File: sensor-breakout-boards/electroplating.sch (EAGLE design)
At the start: 4 parts, among them X1 Type-A Receptacle, X2 Micro Type-B Receptacle

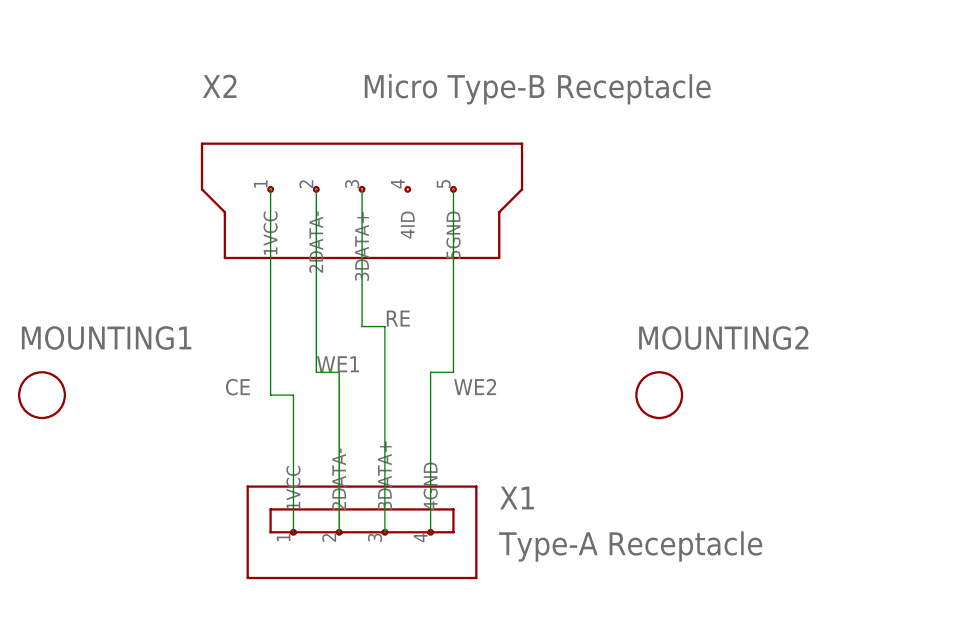
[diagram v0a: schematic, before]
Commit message: three breakout boards complete
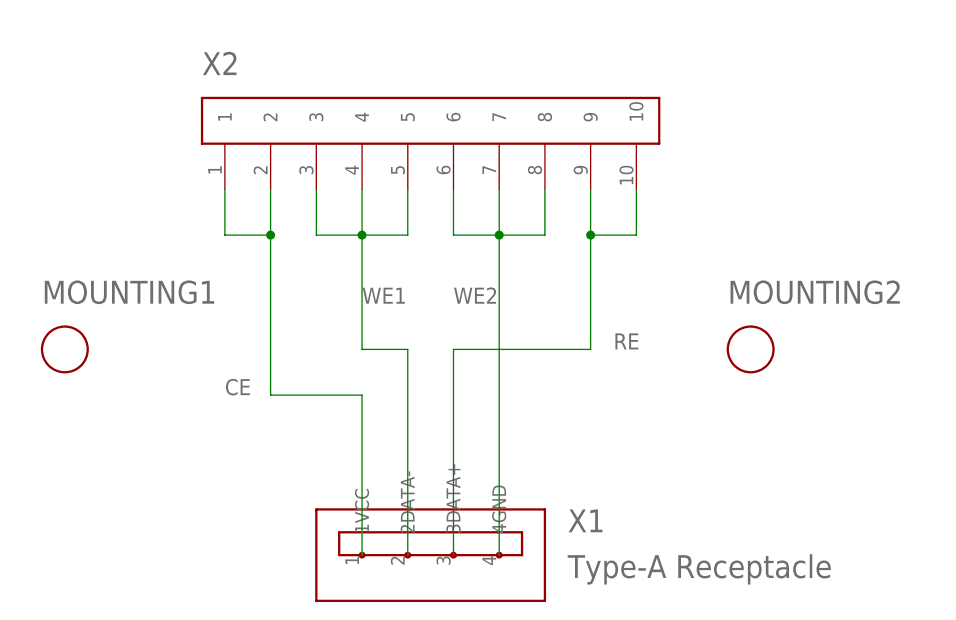
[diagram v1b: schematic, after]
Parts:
- X2: value Micro Type-B Receptacle -> 10-PIN-CONNECTOR; device sensor-breakout-boards:USB-MICRO-TYPE-B-RECEPTACLE -> sensor-breakout-boards:10-PIN-CONNECTOR
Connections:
- net CE: now also X2.1, X2.2; no longer X2.1VCC
- net RE: now also X2.10, X2.9; no longer X2.3DATA+
- net WE1: now also X2.3, X2.4, X2.5; no longer X2.2DATA-
- net WE2: now also X2.6, X2.7, X2.8; no longer X2.5GND
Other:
- moved on the sheet: MOUNTING1, MOUNTING2, X1
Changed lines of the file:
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@@
 <parts>
 <part name="X1" library="sensor-breakout-boards" deviceset="USB-TYPE-A-RECEPTACLE" device="" value="Type-A Receptacle"/>
-<part name="X2" library="sensor-breakout-boards" deviceset="USB-MICRO-TYPE-B-RECEPTACLE" device="" value="Micro Type-B Receptacle"/>
+<part name="X2" library="sensor-breakout-boards" deviceset="10-PIN-CONNECTOR" device=""/>
 <part name="MOUNTING1" library="sensor-breakout-boards" deviceset="M2-MOUNTING-HOLE" device=""/>
 <part name="MOUNTING2" library="sensor-breakout-boards" deviceset="M2-MOUNTING-HOLE" device=""/>
@@
 </plain>
 <instances>
-<instance part="X1" gate="G$1" x="43.18" y="17.78"/>
-<instance part="X2" gate="G$1" x="43.18" y="55.88"/>
-<instance part="MOUNTING1" gate="G$1" x="7.62" y="33.02"/>
-<instance part="MOUNTING2" gate="G$1" x="76.2" y="33.02"/>
+<instance part="X1" gate="G$1" x="50.8" y="15.24"/>
+<instance part="X2" gate="G$1" x="50.8" y="63.5"/>
+<instance part="MOUNTING1" gate="G$1" x="10.16" y="38.1"/>
+<instance part="MOUNTING2" gate="G$1" x="86.36" y="38.1"/>
 </instances>
 <busses>
@@
 <net name="CE" class="0">
 <segment>
+<pinref part="X2" gate="G$1" pin="1"/>
+<wire x1="27.94" y1="55.88" x2="27.94" y2="50.8" width="0.1524" layer="91"/>
+<wire x1="27.94" y1="50.8" x2="33.02" y2="50.8" width="0.1524" layer="91"/>
+<pinref part="X2" gate="G$1" pin="2"/>
+<wire x1="33.02" y1="50.8" x2="33.02" y2="55.88" width="0.1524" layer="91"/>
+<wire x1="33.02" y1="50.8" x2="33.02" y2="33.02" width="0.1524" layer="91"/>
+<junction x="33.02" y="50.8"/>
 <pinref part="X1" gate="G$1" pin="1VCC"/>
-<wire x1="35.56" y1="17.78" x2="35.56" y2="33.02" width="0.1524" layer="91"/>
-<wire x1="35.56" y1="33.02" x2="33.02" y2="33.02" width="0.1524" layer="91"/>
-<pinref part="X2" gate="G$1" pin="1VCC"/>
-<wire x1="33.02" y1="33.02" x2="33.02" y2="55.88" width="0.1524" layer="91"/>
+<wire x1="33.02" y1="33.02" x2="43.18" y2="33.02" width="0.1524" layer="91"/>
+<wire x1="43.18" y1="33.02" x2="43.18" y2="15.24" width="0.1524" layer="91"/>
 <label x="27.94" y="33.02" size="1.778" layer="95"/>
 </segment>
@@
 <net name="WE1" class="0">
 <segment>
-<pinref part="X2" gate="G$1" pin="2DATA-"/>
-<wire x1="38.1" y1="55.88" x2="38.1" y2="35.56" width="0.1524" layer="91"/>
+<pinref part="X2" gate="G$1" pin="3"/>
+<wire x1="38.1" y1="55.88" x2="38.1" y2="50.8" width="0.1524" layer="91"/>
+<wire x1="38.1" y1="50.8" x2="43.18" y2="50.8" width="0.1524" layer="91"/>
+<pinref part="X2" gate="G$1" pin="4"/>
+<wire x1="43.18" y1="50.8" x2="43.18" y2="55.88" width="0.1524" layer="91"/>
+<pinref part="X2" gate="G$1" pin="5"/>
+<wire x1="43.18" y1="50.8" x2="48.26" y2="50.8" width="0.1524" layer="91"/>
+<wire x1="48.26" y1="50.8" x2="48.26" y2="55.88" width="0.1524" layer="91"/>
+<junction x="43.18" y="50.8"/>
+<wire x1="43.18" y1="50.8" x2="43.18" y2="38.1" width="0.1524" layer="91"/>
 <pinref part="X1" gate="G$1" pin="2DATA-"/>
-<wire x1="38.1" y1="35.56" x2="40.64" y2="35.56" width="0.1524" layer="91"/>
-<wire x1="40.64" y1="35.56" x2="40.64" y2="17.78" width="0.1524" layer="91"/>
-<label x="38.1" y="35.56" size="1.778" layer="95"/>
+<wire x1="43.18" y1="38.1" x2="48.26" y2="38.1" width="0.1524" layer="91"/>
+<wire x1="48.26" y1="38.1" x2="48.26" y2="15.24" width="0.1524" layer="91"/>
+<label x="43.18" y="43.18" size="1.778" layer="95"/>
+</segment>
+</net>
+<net name="WE2" class="0">
+<segment>
+<pinref part="X2" gate="G$1" pin="6"/>
+<wire x1="53.34" y1="55.88" x2="53.34" y2="50.8" width="0.1524" layer="91"/>
+<wire x1="53.34" y1="50.8" x2="58.42" y2="50.8" width="0.1524" layer="91"/>
+<pinref part="X2" gate="G$1" pin="7"/>
+<wire x1="58.42" y1="50.8" x2="58.42" y2="55.88" width="0.1524" layer="91"/>
+<wire x1="58.42" y1="50.8" x2="63.5" y2="50.8" width="0.1524" layer="91"/>
+<junction x="58.42" y="50.8"/>
+<pinref part="X2" gate="G$1" pin="8"/>
+<wire x1="63.5" y1="50.8" x2="63.5" y2="55.88" width="0.1524" layer="91"/>
+<pinref part="X1" gate="G$1" pin="4GND"/>
+<wire x1="58.42" y1="50.8" x2="58.42" y2="15.24" width="0.1524" layer="91"/>
+<label x="53.34" y="43.18" size="1.778" layer="95"/>
 </segment>
 </net>
 <net name="RE" class="0">
 <segment>
-<pinref part="X2" gate="G$1" pin="3DATA+"/>
-<wire x1="43.18" y1="55.88" x2="43.18" y2="40.64" width="0.1524" layer="91"/>
+<pinref part="X2" gate="G$1" pin="9"/>
+<wire x1="68.58" y1="55.88" x2="68.58" y2="50.8" width="0.1524" layer="91"/>
+<wire x1="68.58" y1="50.8" x2="73.66" y2="50.8" width="0.1524" layer="91"/>
+<pinref part="X2" gate="G$1" pin="10"/>
+<wire x1="73.66" y1="50.8" x2="73.66" y2="55.88" width="0.1524" layer="91"/>
+<wire x1="68.58" y1="50.8" x2="68.58" y2="38.1" width="0.1524" layer="91"/>
+<junction x="68.58" y="50.8"/>
 <pinref part="X1" gate="G$1" pin="3DATA+"/>
-<wire x1="43.18" y1="40.64" x2="45.72" y2="40.64" width="0.1524" layer="91"/>
-<wire x1="45.72" y1="40.64" x2="45.72" y2="17.78" width="0.1524" layer="91"/>
-<label x="45.72" y="40.64" size="1.778" layer="95"/>
+<wire x1="68.58" y1="38.1" x2="53.34" y2="38.1" width="0.1524" layer="91"/>
+<wire x1="53.34" y1="38.1" x2="53.34" y2="15.24" width="0.1524" layer="91"/>
+<label x="71.12" y="38.1" size="1.778" layer="95"/>
 </segment>
 </net>
-<net name="WE2" class="0">
-<segment>
-<pinref part="X2" gate="G$1" pin="5GND"/>
-<wire x1="53.34" y1="55.88" x2="53.34" y2="35.56" width="0.1524" layer="91"/>
-<pinref part="X1" gate="G$1" pin="4GND"/>
-<wire x1="53.34" y1="35.56" x2="50.8" y2="35.56" width="0.1524" layer="91"/>
-<wire x1="50.8" y1="35.56" x2="50.8" y2="17.78" width="0.1524" layer="91"/>
-<label x="53.34" y="33.02" size="1.778" layer="95"/>
-</segment>
-</net>

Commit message: made changes discussed at meeting
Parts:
- added X3, X4, X5: 2-PIN-CONNECTOR, sensor-breakout-boards:2-PIN-CONNECTOR
- X2: value 10-PIN-CONNECTOR -> 2-PIN-CONNECTOR; device sensor-breakout-boards:10-PIN-CONNECTOR -> sensor-breakout-boards:2-PIN-CONNECTOR
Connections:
- net RE: now also X4.1, X4.2; no longer X2.10, X2.9
- net WE1: now also X1.4GND, X5.1, X5.2; no longer X1.2DATA-, X2.3, X2.4, X2.5
- net WE2: now also X1.2DATA-, X3.1, X3.2; no longer X1.4GND, X2.6, X2.7, X2.8
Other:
- moved on the sheet: MOUNTING1, MOUNTING2
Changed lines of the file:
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@@
 <parts>
 <part name="X1" library="sensor-breakout-boards" deviceset="USB-TYPE-A-RECEPTACLE" device="" value="Type-A Receptacle"/>
-<part name="X2" library="sensor-breakout-boards" deviceset="10-PIN-CONNECTOR" device=""/>
 <part name="MOUNTING1" library="sensor-breakout-boards" deviceset="M2-MOUNTING-HOLE" device=""/>
 <part name="MOUNTING2" library="sensor-breakout-boards" deviceset="M2-MOUNTING-HOLE" device=""/>
+<part name="X2" library="sensor-breakout-boards" deviceset="2-PIN-CONNECTOR" device=""/>
+<part name="X3" library="sensor-breakout-boards" deviceset="2-PIN-CONNECTOR" device=""/>
+<part name="X4" library="sensor-breakout-boards" deviceset="2-PIN-CONNECTOR" device=""/>
+<part name="X5" library="sensor-breakout-boards" deviceset="2-PIN-CONNECTOR" device=""/>
 </parts>
 <sheets>
@@
 <instances>
 <instance part="X1" gate="G$1" x="50.8" y="15.24"/>
-<instance part="X2" gate="G$1" x="50.8" y="63.5"/>
-<instance part="MOUNTING1" gate="G$1" x="10.16" y="38.1"/>
-<instance part="MOUNTING2" gate="G$1" x="86.36" y="38.1"/>
+<instance part="MOUNTING1" gate="G$1" x="10.16" y="20.32"/>
+<instance part="MOUNTING2" gate="G$1" x="83.82" y="30.48"/>
+<instance part="X2" gate="G$1" x="25.4" y="63.5"/>
+<instance part="X3" gate="G$1" x="40.64" y="63.5"/>
+<instance part="X4" gate="G$1" x="55.88" y="63.5"/>
+<instance part="X5" gate="G$1" x="71.12" y="63.5"/>
 </instances>
 <busses>
@@
 <net name="CE" class="0">
 <segment>
+<wire x1="27.94" y1="58.42" x2="27.94" y2="53.34" width="0.1524" layer="91"/>
+<pinref part="X1" gate="G$1" pin="1VCC"/>
+<wire x1="27.94" y1="53.34" x2="27.94" y2="33.02" width="0.1524" layer="91"/>
+<wire x1="27.94" y1="33.02" x2="43.18" y2="33.02" width="0.1524" layer="91"/>
+<wire x1="43.18" y1="33.02" x2="43.18" y2="15.24" width="0.1524" layer="91"/>
+<label x="22.86" y="48.26" size="1.778" layer="95"/>
+<pinref part="X2" gate="G$1" pin="2"/>
 <pinref part="X2" gate="G$1" pin="1"/>
-<wire x1="27.94" y1="55.88" x2="27.94" y2="50.8" width="0.1524" layer="91"/>
-<wire x1="27.94" y1="50.8" x2="33.02" y2="50.8" width="0.1524" layer="91"/>
-<pinref part="X2" gate="G$1" pin="2"/>
-<wire x1="33.02" y1="50.8" x2="33.02" y2="55.88" width="0.1524" layer="91"/>
-<wire x1="33.02" y1="50.8" x2="33.02" y2="33.02" width="0.1524" layer="91"/>
-<junction x="33.02" y="50.8"/>
-<pinref part="X1" gate="G$1" pin="1VCC"/>
-<wire x1="33.02" y1="33.02" x2="43.18" y2="33.02" width="0.1524" layer="91"/>
-<wire x1="43.18" y1="33.02" x2="43.18" y2="15.24" width="0.1524" layer="91"/>
-<label x="27.94" y="33.02" size="1.778" layer="95"/>
+<wire x1="22.86" y1="58.42" x2="22.86" y2="53.34" width="0.1524" layer="91"/>
+<wire x1="22.86" y1="53.34" x2="27.94" y2="53.34" width="0.1524" layer="91"/>
+<junction x="27.94" y="53.34"/>
+</segment>
+</net>
+<net name="WE2" class="0">
+<segment>
+<wire x1="43.18" y1="58.42" x2="43.18" y2="53.34" width="0.1524" layer="91"/>
+<pinref part="X1" gate="G$1" pin="2DATA-"/>
+<wire x1="43.18" y1="53.34" x2="43.18" y2="38.1" width="0.1524" layer="91"/>
+<wire x1="43.18" y1="38.1" x2="48.26" y2="38.1" width="0.1524" layer="91"/>
+<wire x1="48.26" y1="38.1" x2="48.26" y2="15.24" width="0.1524" layer="91"/>
+<label x="38.1" y="48.26" size="1.778" layer="95"/>
+<pinref part="X3" gate="G$1" pin="2"/>
+<pinref part="X3" gate="G$1" pin="1"/>
+<wire x1="38.1" y1="58.42" x2="38.1" y2="53.34" width="0.1524" layer="91"/>
+<wire x1="38.1" y1="53.34" x2="43.18" y2="53.34" width="0.1524" layer="91"/>
+<junction x="43.18" y="53.34"/>
 </segment>
 </net>
 <net name="WE1" class="0">
 <segment>
-<pinref part="X2" gate="G$1" pin="3"/>
-<wire x1="38.1" y1="55.88" x2="38.1" y2="50.8" width="0.1524" layer="91"/>
-<wire x1="38.1" y1="50.8" x2="43.18" y2="50.8" width="0.1524" layer="91"/>
-<pinref part="X2" gate="G$1" pin="4"/>
-<wire x1="43.18" y1="50.8" x2="43.18" y2="55.88" width="0.1524" layer="91"/>
-<pinref part="X2" gate="G$1" pin="5"/>
-<wire x1="43.18" y1="50.8" x2="48.26" y2="50.8" width="0.1524" layer="91"/>
-<wire x1="48.26" y1="50.8" x2="48.26" y2="55.88" width="0.1524" layer="91"/>
-<junction x="43.18" y="50.8"/>
-<wire x1="43.18" y1="50.8" x2="43.18" y2="38.1" width="0.1524" layer="91"/>
-<pinref part="X1" gate="G$1" pin="2DATA-"/>
-<wire x1="43.18" y1="38.1" x2="48.26" y2="38.1" width="0.1524" layer="91"/>
-<wire x1="48.26" y1="38.1" x2="48.26" y2="15.24" width="0.1524" layer="91"/>
-<label x="43.18" y="43.18" size="1.778" layer="95"/>
-</segment>
-</net>
-<net name="WE2" class="0">
-<segment>
-<pinref part="X2" gate="G$1" pin="6"/>
-<wire x1="53.34" y1="55.88" x2="53.34" y2="50.8" width="0.1524" layer="91"/>
-<wire x1="53.34" y1="50.8" x2="58.42" y2="50.8" width="0.1524" layer="91"/>
-<pinref part="X2" gate="G$1" pin="7"/>
-<wire x1="58.42" y1="50.8" x2="58.42" y2="55.88" width="0.1524" layer="91"/>
-<wire x1="58.42" y1="50.8" x2="63.5" y2="50.8" width="0.1524" layer="91"/>
-<junction x="58.42" y="50.8"/>
-<pinref part="X2" gate="G$1" pin="8"/>
-<wire x1="63.5" y1="50.8" x2="63.5" y2="55.88" width="0.1524" layer="91"/>
 <pinref part="X1" gate="G$1" pin="4GND"/>
-<wire x1="58.42" y1="50.8" x2="58.42" y2="15.24" width="0.1524" layer="91"/>
-<label x="53.34" y="43.18" size="1.778" layer="95"/>
+<wire x1="58.42" y1="38.1" x2="58.42" y2="15.24" width="0.1524" layer="91"/>
+<label x="68.58" y="48.26" size="1.778" layer="95"/>
+<pinref part="X5" gate="G$1" pin="1"/>
+<wire x1="58.42" y1="38.1" x2="68.58" y2="38.1" width="0.1524" layer="91"/>
+<wire x1="68.58" y1="38.1" x2="68.58" y2="53.34" width="0.1524" layer="91"/>
+<pinref part="X5" gate="G$1" pin="2"/>
+<wire x1="68.58" y1="53.34" x2="68.58" y2="58.42" width="0.1524" layer="91"/>
+<wire x1="68.58" y1="53.34" x2="73.66" y2="53.34" width="0.1524" layer="91"/>
+<wire x1="73.66" y1="53.34" x2="73.66" y2="58.42" width="0.1524" layer="91"/>
+<junction x="68.58" y="53.34"/>
 </segment>
 </net>
 <net name="RE" class="0">
 <segment>
-<pinref part="X2" gate="G$1" pin="9"/>
-<wire x1="68.58" y1="55.88" x2="68.58" y2="50.8" width="0.1524" layer="91"/>
-<wire x1="68.58" y1="50.8" x2="73.66" y2="50.8" width="0.1524" layer="91"/>
-<pinref part="X2" gate="G$1" pin="10"/>
-<wire x1="73.66" y1="50.8" x2="73.66" y2="55.88" width="0.1524" layer="91"/>
-<wire x1="68.58" y1="50.8" x2="68.58" y2="38.1" width="0.1524" layer="91"/>
-<junction x="68.58" y="50.8"/>
 <pinref part="X1" gate="G$1" pin="3DATA+"/>
-<wire x1="68.58" y1="38.1" x2="53.34" y2="38.1" width="0.1524" layer="91"/>
-<wire x1="53.34" y1="38.1" x2="53.34" y2="15.24" width="0.1524" layer="91"/>
-<label x="71.12" y="38.1" size="1.778" layer="95"/>
+<wire x1="53.34" y1="58.42" x2="53.34" y2="53.34" width="0.1524" layer="91"/>
+<label x="53.34" y="48.26" size="1.778" layer="95"/>
+<pinref part="X4" gate="G$1" pin="1"/>
+<pinref part="X4" gate="G$1" pin="2"/>
+<wire x1="53.34" y1="53.34" x2="53.34" y2="15.24" width="0.1524" layer="91"/>
+<wire x1="53.34" y1="53.34" x2="58.42" y2="53.34" width="0.1524" layer="91"/>
+<wire x1="58.42" y1="53.34" x2="58.42" y2="58.42" width="0.1524" layer="91"/>
+<junction x="53.34" y="53.34"/>
 </segment>
 </net>
